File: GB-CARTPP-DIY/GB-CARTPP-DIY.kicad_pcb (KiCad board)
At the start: 2 copper layers, 100 x 100 mm, 31 parts, among them J1 USB_B, J2 ICSP, J3 GameBoy_Cartridge_MountingPin, Q1 PMOS, U1 PIC18F45K50-IP

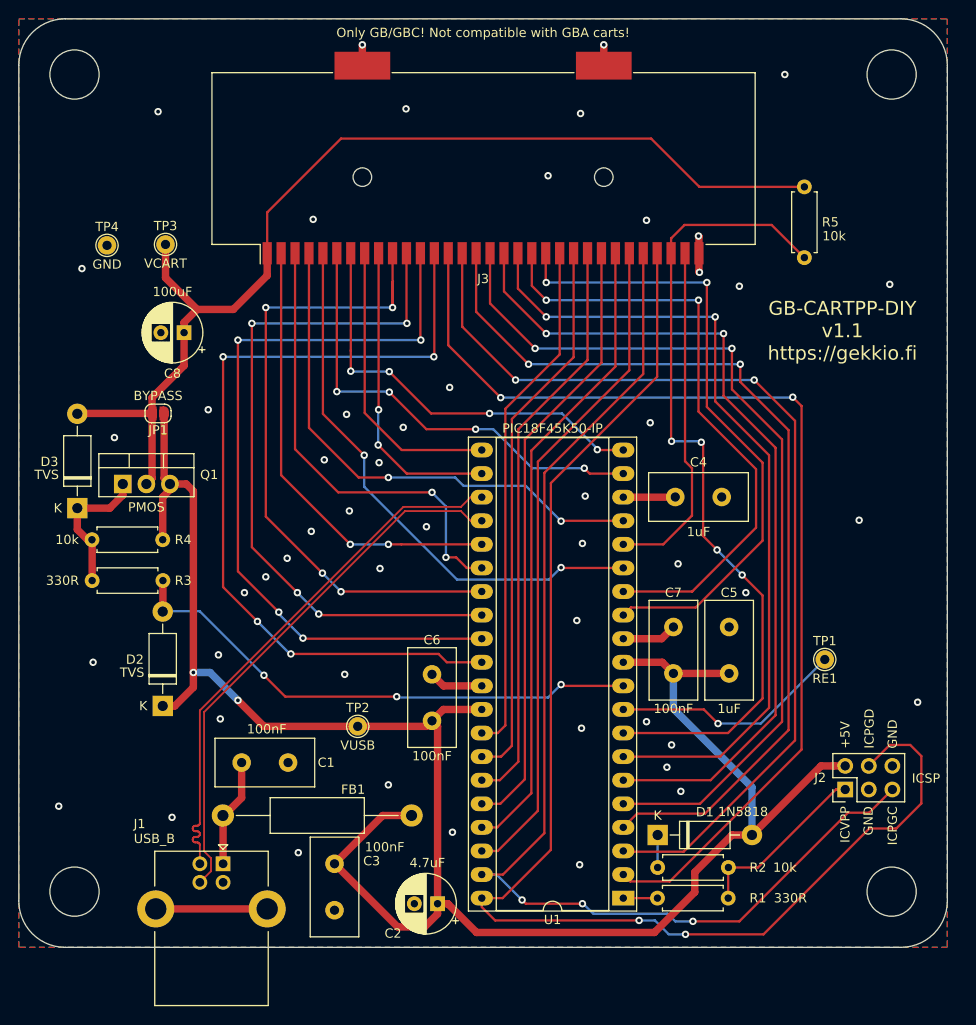
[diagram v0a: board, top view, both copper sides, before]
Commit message: Upgrade most projects to KiCad 6
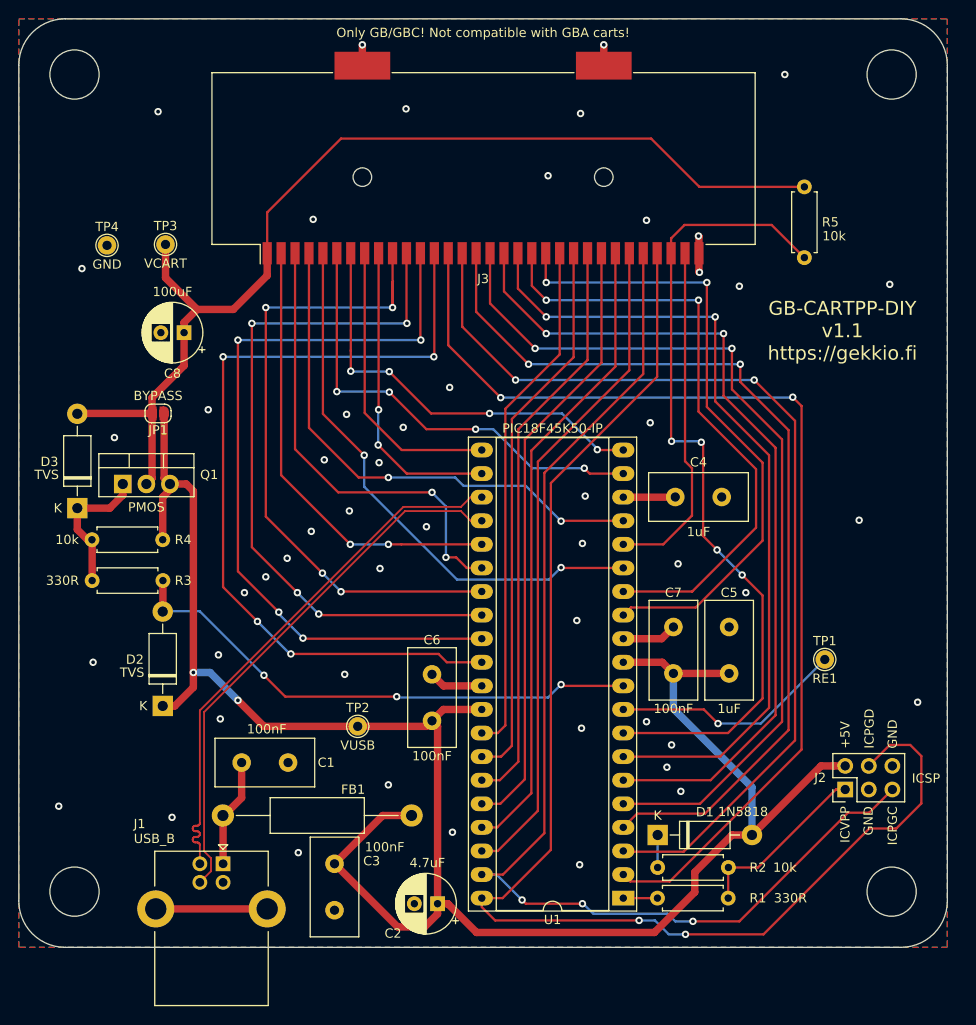
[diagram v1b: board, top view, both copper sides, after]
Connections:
- net /~CS renamed /~{CS}
- net /~RD renamed /~{RD}
- net /~RES renamed /~{RES}
- net /~WR renamed /~{WR}
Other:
- net class Default removed
